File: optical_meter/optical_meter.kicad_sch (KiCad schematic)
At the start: 1 part, among them U1 Pico

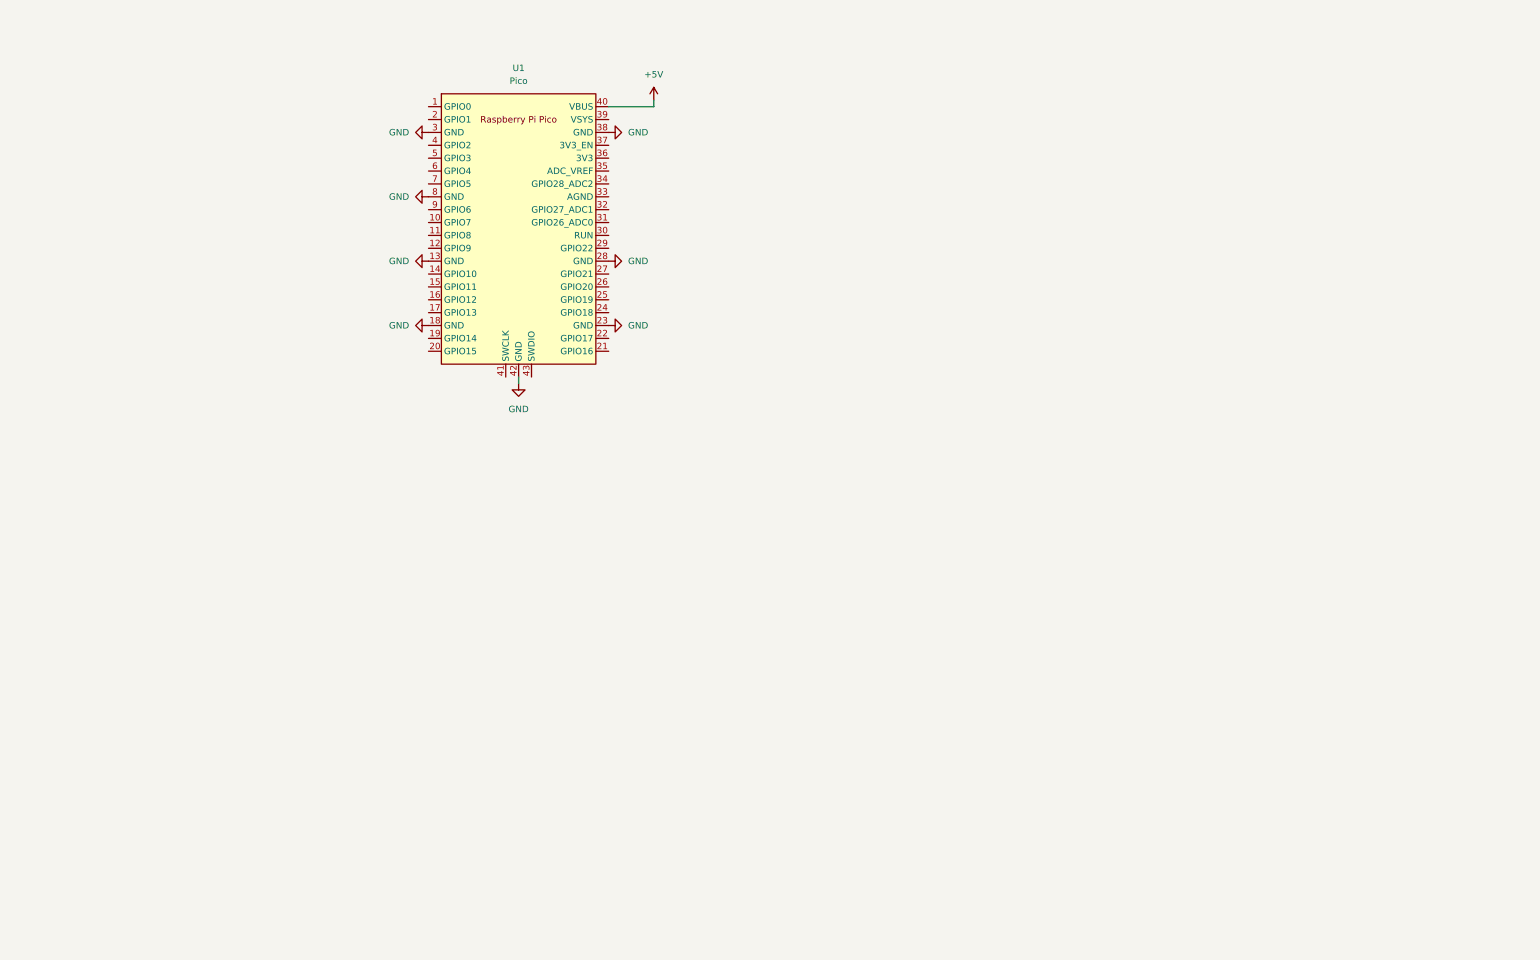
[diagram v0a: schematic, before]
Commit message: Adding MH, Power OK diodes, new Goldping socket 3D model for RaspPi, SFP connectors with cage 3D model
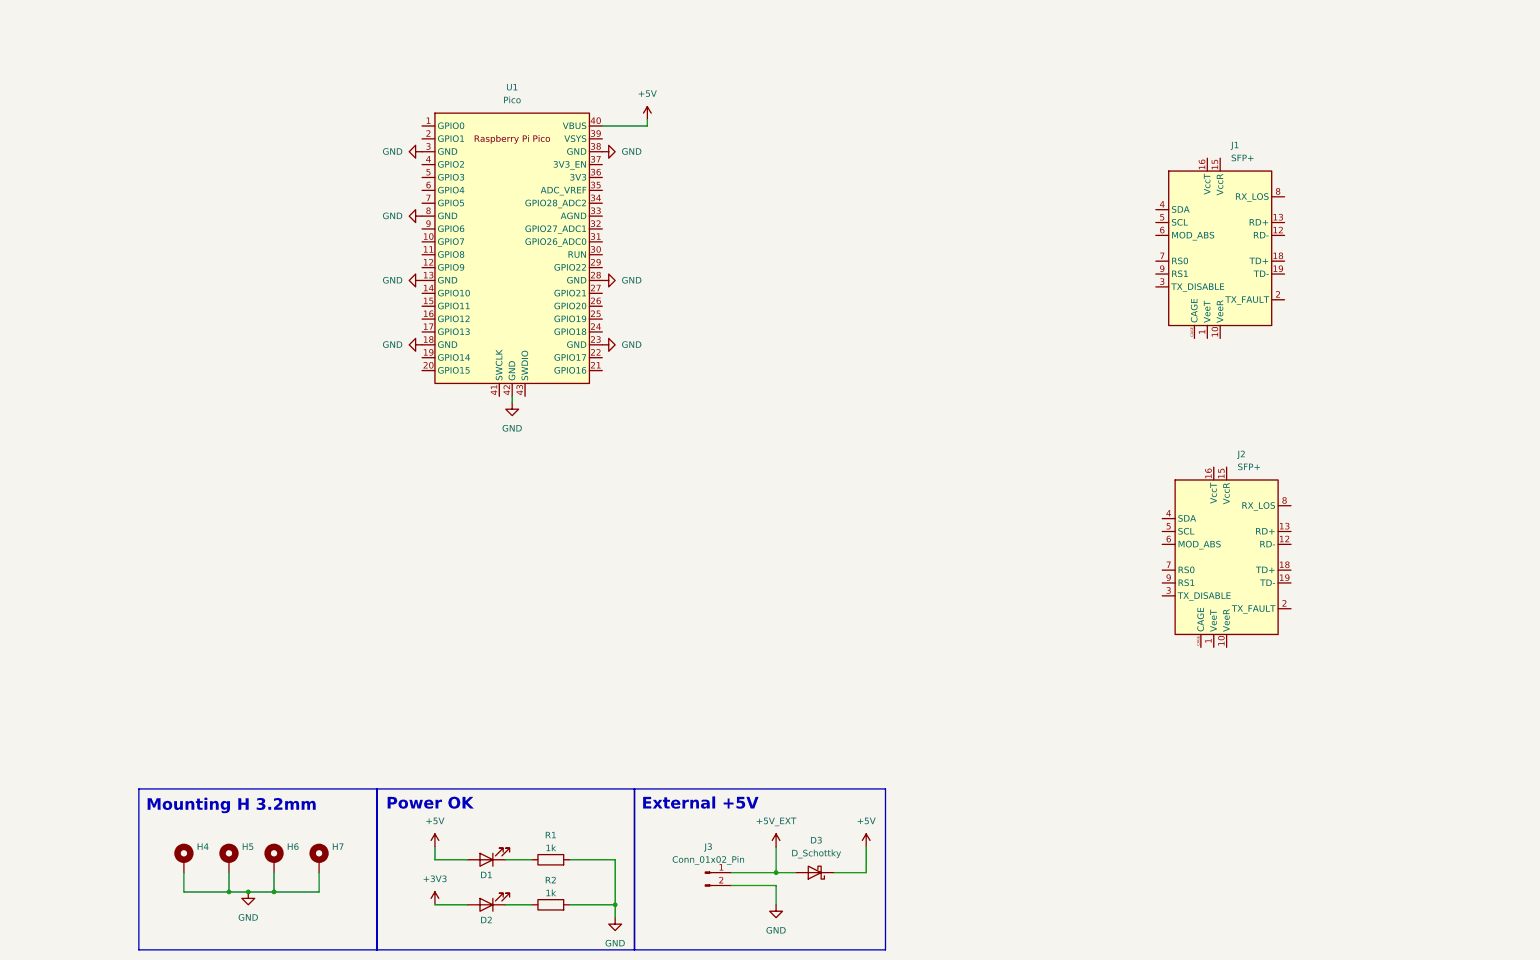
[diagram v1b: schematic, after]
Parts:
- added D1, D2: LED, symbol Device:LED
- added D3: D_Schottky, symbol Device:D_Schottky
- added H4, H5, H6, H7: ~, MountingHole:MountingHole_3.2mm_M3_DIN965_Pad, symbol Mechanical:MountingHole_Pad
- added J1, J2: SFP+, SFP:Connector_SFP_and_Cage, symbol Interface_Optical:SFP+
- added J3: Conn_01x02_Pin, symbol Connector:Conn_01x02_Pin
- added R1, R2: 1k, symbol Device:R
- U1: now left out of the parts list
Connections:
- net +5V: now also D1.2 (A), D3.1 (K)
- net GND: now also H4.1, H5.1, H6.1, H7.1, J3.2 (Pin_2), R1.2, R2.2
- new net: J1.1 (VeeT), J1.17 (VeeT), J1.20 (VeeT)
- new net: J1.10 (VeeR), J1.11 (VeeR), J1.14 (VeeR)
- new net: D2.1 (K), R2.1
- new net: D1.1 (K), R1.1
- new net: J2.1 (VeeT), J2.17 (VeeT), J2.20 (VeeT)
- new net: J2.10 (VeeR), J2.11 (VeeR), J2.14 (VeeR)
- new net +3V3: D2.2 (A)
- new net +5V_EXT: D3.2 (A), J3.1 (Pin_1)
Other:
- note added: "External +5V"
- note added: "Mounting H 3.2mm"
- note added: "Power OK"
- company: (none) -> Filip Kulka
- title: (none) -> Optical Power Analyzer
- moved on the sheet: U1

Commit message: Finished schematic (v1.0)
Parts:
- removed D3: D_Schottky, symbol Device:D_Schottky
- removed U1: Pico, MCU_RaspberryPi_and_Boards:RPi_Pico_SMD_TH, symbol MCU_RaspberryPi_and_Boards:Pico
- added C1, C16, C7: 4u7, Capacitor_SMD:C_0603_1608Metric, symbol Device:C
- added C10, C11, C12, C13, C14, C15, C2, C3, C4, C5, C6, C8, C9: 100n, Capacitor_SMD:C_0603_1608Metric, symbol Device:C
- added L1, L2, L3, L4: 1u, Inductor_SMD:L_0805_2012Metric_Pad1.15x1.40mm_HandSolder, symbol Device:L
- added R10, R9: 100, Resistor_SMD:R_0603_1608Metric_Pad0.98x0.95mm_HandSolder, symbol Device:R
- added R11, R3, R4, R6, R7, R8: 4k7, Resistor_SMD:R_0603_1608Metric_Pad0.98x0.95mm_HandSolder, symbol Device:R
- added U2: FIN1002M5X, LVDS_RX_lib:SOT95P280X140-5N, symbol TTL --{gt} LVDS (FIN1002M5X):FIN1002M5X
- added U3: FIN1001M5X, LVDS_RX_lib:SOT95P280X140-5N, symbol LVDS --{gt} TTL (FIN1001M5X):FIN1001M5X
- D1, D2: footprint (none) -> Diode_SMD:D_0603_1608Metric
- J3: footprint (none) -> Connector_PinHeader_2.54mm:PinHeader_1x02_P2.54mm_Vertical
- R1, R2: footprint (none) -> Resistor_SMD:R_0603_1608Metric_Pad0.98x0.95mm_HandSolder
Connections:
- net +5V_EXT is gone; now on net +5V: J3.1 (Pin_1)
- net +3V3: now also C1.1, C14.2, C4.2, C5.2, C7.1, C9.2, L1.2, L2.2, L3.2, L4.2, R11.2, R3.1, R4.2, R6.2, R7.2, R8.1, U2.1 (VCC), U3.1 (VCC)
- net +5V: now also C15.1, C16.1
- net GND: now also J1.1 (VeeT), J1.10 (VeeR), J1.11 (VeeR), J1.14 (VeeR), J1.17 (VeeT), J1.20 (VeeT), J1.6 (MOD_ABS), J1.CAGE, J2.1 (VeeT), J2.10 (VeeR), J2.11 (VeeR), J2.14 (VeeR), J2.17 (VeeT), J2.20 (VeeT), J2.6 (MOD_ABS), J2.CAGE, C1.2, C14.1, C15.2, C16.2, C2.2, C3.1, C4.1, C5.1, C6.1, C7.2, C8.2, C9.1, U2.2 (GND), U3.2 (GND)
- net at J1.15 (VccR): now also C2.1, L2.1
- net at J1.16 (VccT): now also C3.2, L1.1
- net TD0+: now reaches J1.18 (TD+)
- net TD0+: now also C10.2
- net TD0-: now reaches J1.19 (TD-)
- net TD0-: now also C11.2
- net at J1.2 (TX_FAULT): now also R3.2
- net TX_DISABLE0: now reaches J1.3 (TX_DISABLE)
- net TX_DISABLE0: now also R11.1
- net SDA0: now reaches J1.4 (SDA)
- net SCL0: now reaches J1.5 (SCL)
- net RS00: now reaches J1.7 (RS0)
- net at J1.8 (RX_LOS): now also R4.1
- net RS10: now reaches J1.9 (RS1)
- net RD1-: now reaches J2.12 (RD-)
- net RD1-: now also C12.2
- net RD1+: now reaches J2.13 (RD+)
- net RD1+: now also C13.2
- net at J2.15 (VccR): now also C8.1, L4.1
- net at J2.16 (VccT): now also C6.2, L3.1
- net at J2.2 (TX_FAULT): now also R8.2
- net TX_DISABLE1: now reaches J2.3 (TX_DISABLE)
- net TX_DISABLE1: now also R6.1
- net SDA1: now reaches J2.4 (SDA)
- net SCL1: now reaches J2.5 (SCL)
- net RS01: now reaches J2.7 (RS0)
- net at J2.8 (RX_LOS): now also R7.1
- net RS11: now reaches J2.9 (RS1)
- new net: C10.1, R9.1, U3.4 (DOUT+)
- new net: C11.1, R9.2, U3.3 (DOUT-)
- new net: C12.1, R10.1, U2.4 (RIN-)
- new net: C13.1, R10.2, U2.3 (RIN+)
- new net Rpi_RX: U2.5 (ROUT)
- new net Rpi_TX: U3.5 (DIN)
- no-connect marks 0 -> 4
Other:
- added sheet RaspberryPi Pico (RaspiPico.kicad_sch)
- note added: "LVDS --> LVTTL"
- note added: "LVTTL --> LVDS"
- note added: "SFP0 (TX)"
- note added: "SFP1 (RX)"
- moved on the sheet: J1

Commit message: Fixed pullup connections at TX_FAULT and R_LOS pins
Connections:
- net +3V3: no longer R8.1
- net TX_FAULT0: now reaches J1.2 (TX_FAULT), R3.2
- net RX_LOS0: now reaches J1.8 (RX_LOS), R4.1
- net TX_FAULT1: now reaches J2.2 (TX_FAULT), R8.2
- net RX_LOS1: now reaches J2.8 (RX_LOS), R7.1
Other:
- moved on the sheet: R3, R4, R7, R8

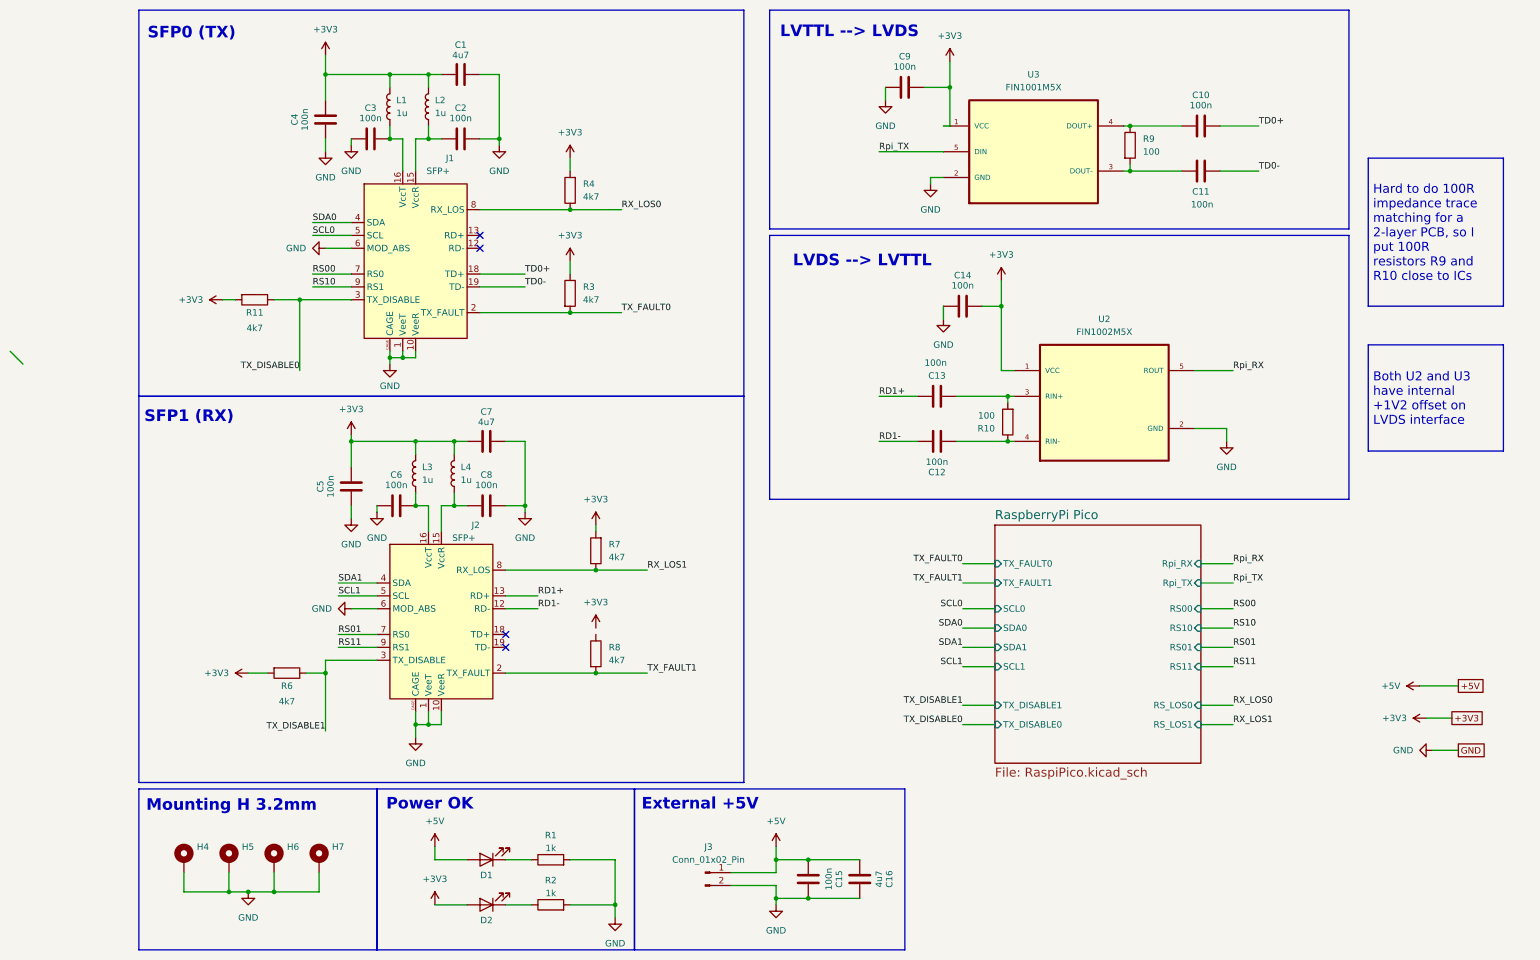
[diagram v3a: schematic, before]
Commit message: Adding voltage divider bias for +1V2 at RD1 pins of component U2
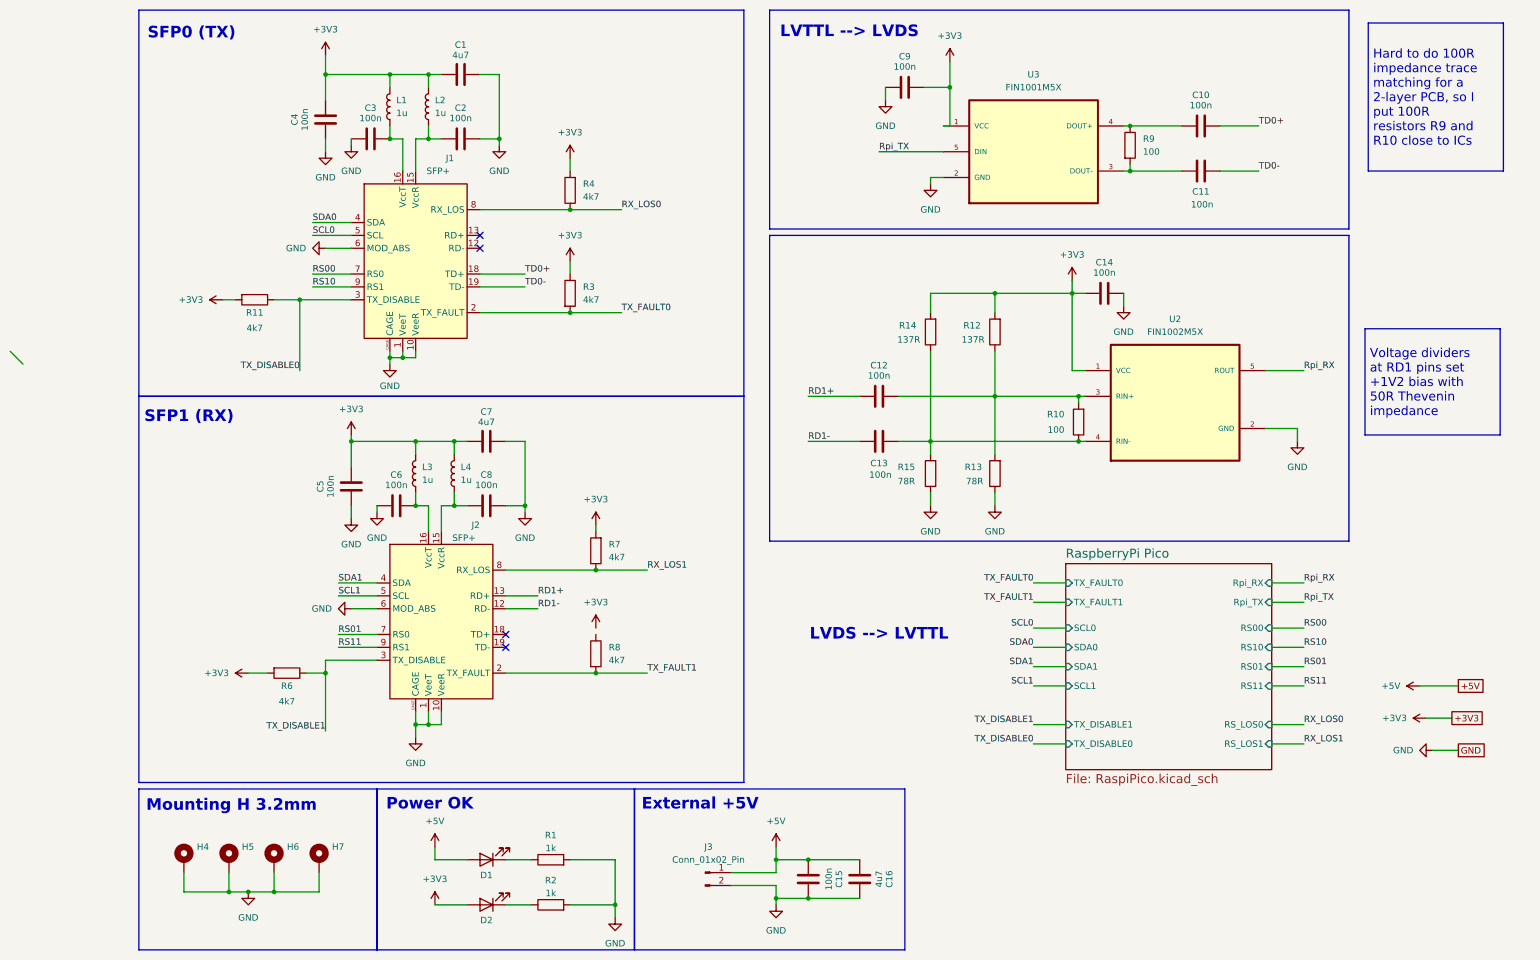
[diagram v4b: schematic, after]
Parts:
- added R12, R14: 137R, Resistor_SMD:R_0603_1608Metric_Pad0.98x0.95mm_HandSolder, symbol Device:R
- added R13, R15: 78R, Resistor_SMD:R_0603_1608Metric_Pad0.98x0.95mm_HandSolder, symbol Device:R
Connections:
- net +3V3: now also R12.2, R14.2
- net GND: now also R13.1, R15.1
- net RD1+: now also C12.1; no longer C13.2
- net RD1-: now also C13.1; no longer C12.2
- net at R10.1, U2.4 (RIN-): now also C13.2, R14.1, R15.2; no longer C12.1
- net at R10.2, U2.3 (RIN+): now also C12.2, R12.1, R13.2; no longer C13.1
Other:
- moved on the sheet: C14, R10, U2
